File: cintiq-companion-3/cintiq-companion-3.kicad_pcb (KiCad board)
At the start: 2 copper layers, 6 parts, among them J3 13HD_buttonboard, X1 13HD_eDP, X2 13HD_penpanel

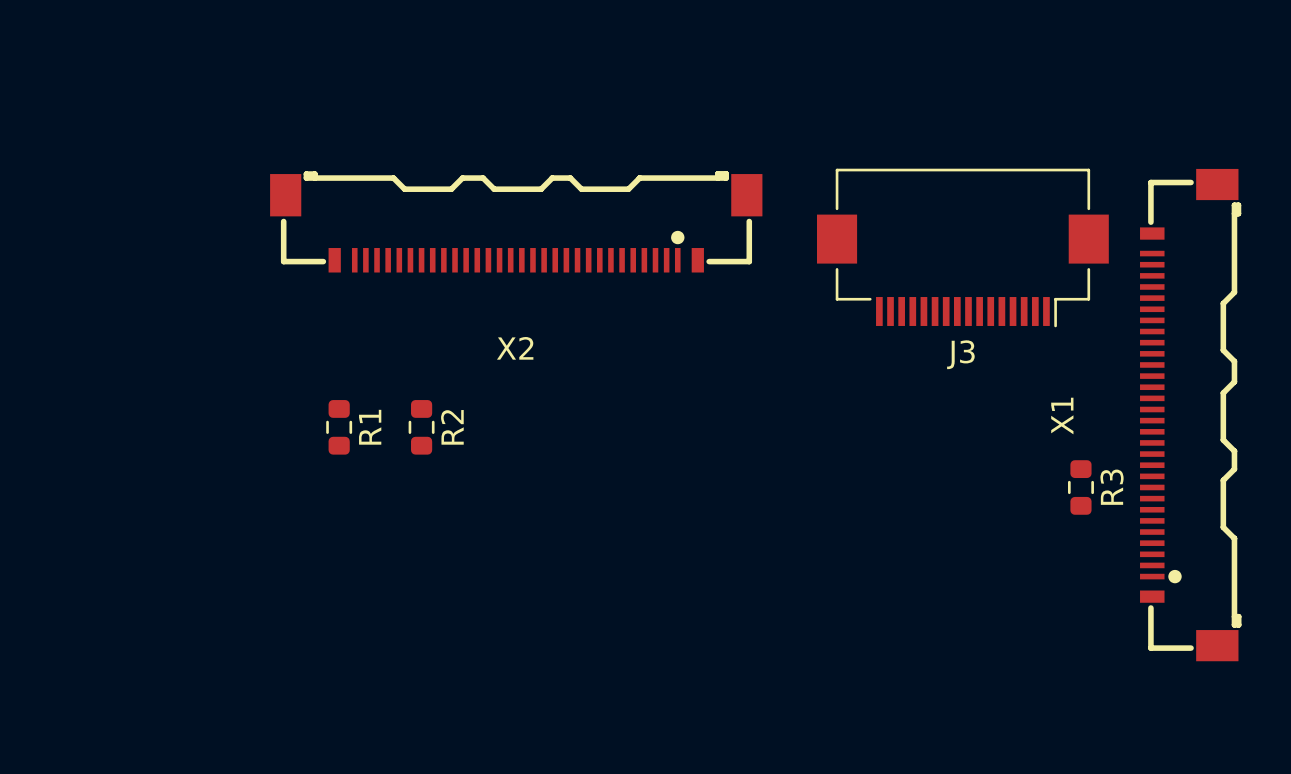
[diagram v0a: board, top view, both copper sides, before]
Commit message: Added touch panel USB footprint
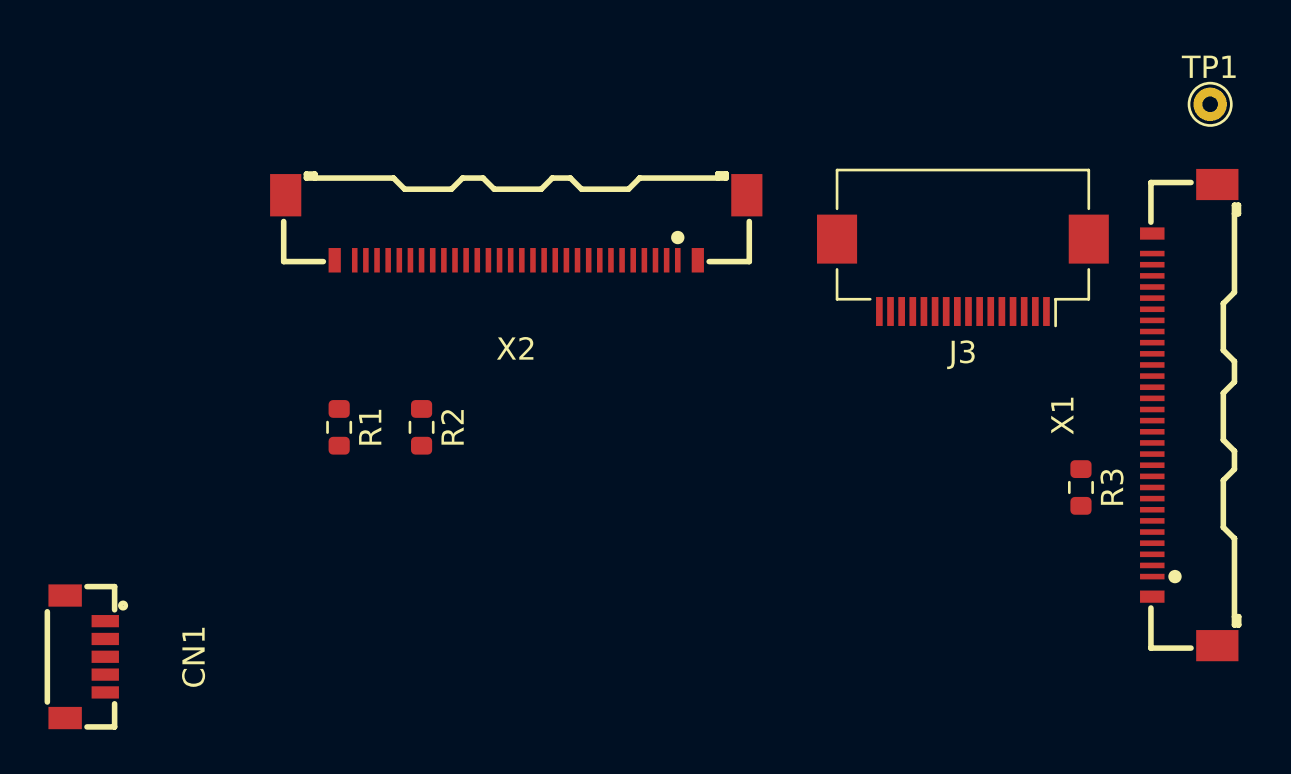
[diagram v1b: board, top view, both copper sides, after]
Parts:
- added CN1: 13HD_fingerpanel, A_my_stuff:minitek5p0.8mm, F.Cu at (144.9, 96.9)
- added TP1: Something, TestPoint:TestPoint_THTPad_D1.5mm_Drill0.7mm, F.Cu at (195.4, 72.1)

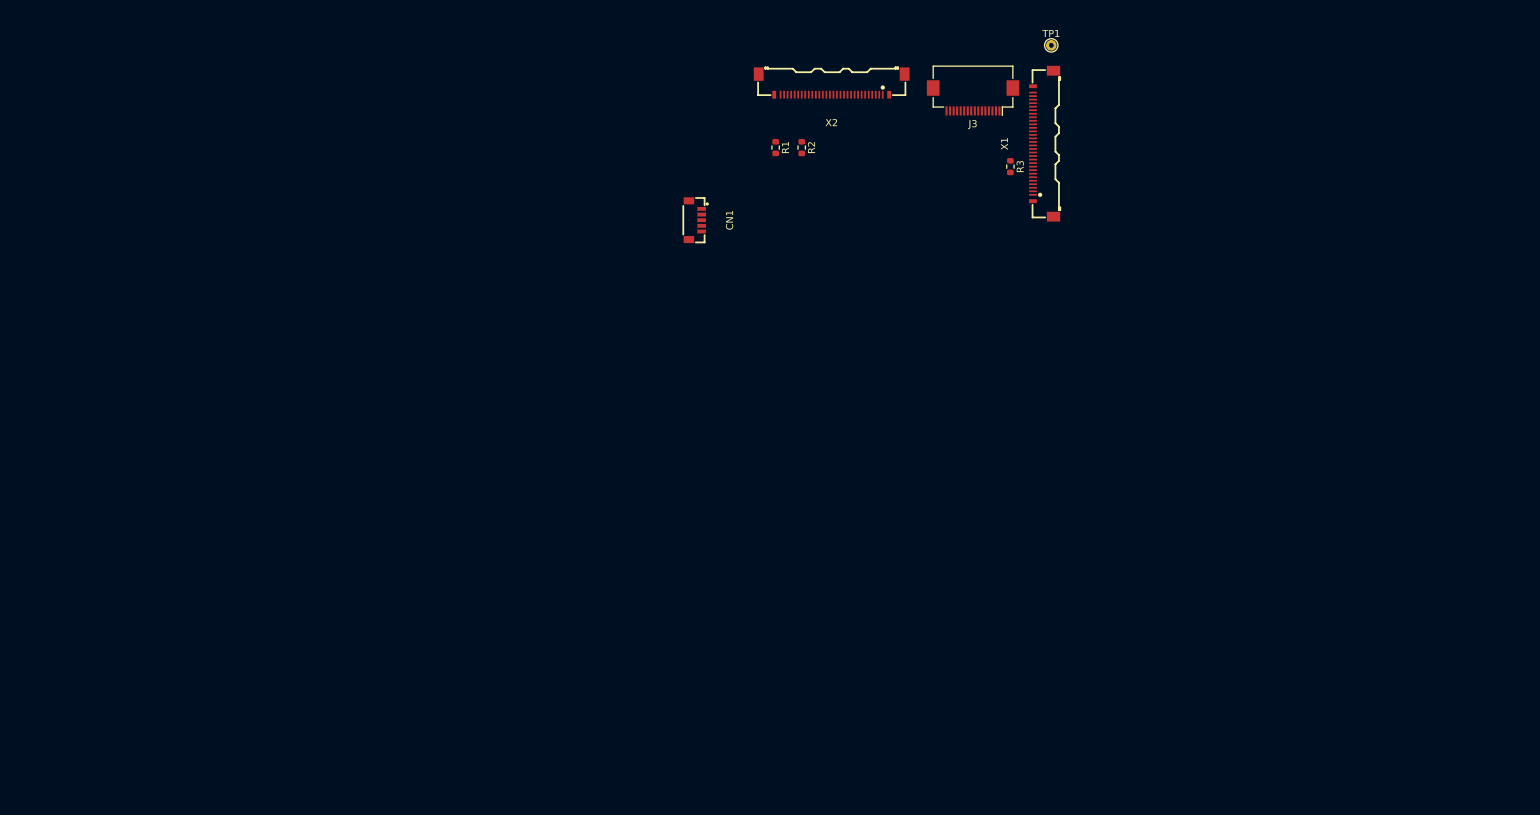
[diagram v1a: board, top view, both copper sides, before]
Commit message: Approximate connector placement done
Big board :skull:
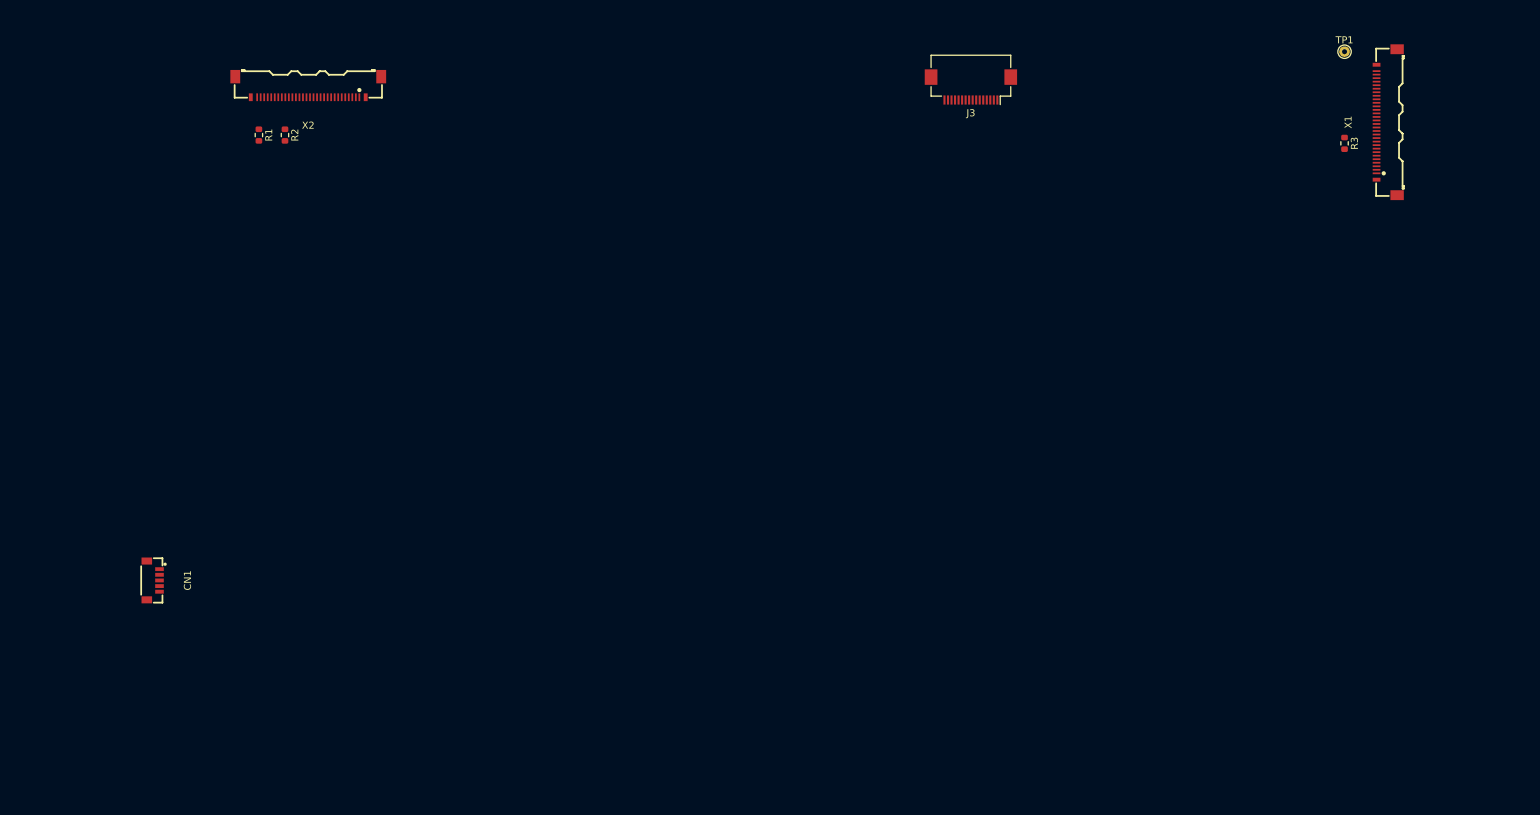
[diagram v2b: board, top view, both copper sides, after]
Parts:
- moved CN1 92.3 mm to (68.0, 148.0)
- moved X2 74.3 mm to (90.0, 78.0)
- moved R1 73.3 mm to (83.0, 84.8)
- moved R2 73.3 mm to (86.7, 84.8)
- moved X1 48.8 mm to (243.0, 83.0)
- moved R3 47.5 mm to (237.0, 86.0)
- moved TP1 41.6 mm to (237.0, 73.0)
- moved J3 1.58 mm to (184.0, 78.0)
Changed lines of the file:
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@@
 	(footprint "TestPoint:TestPoint_THTPad_D1.5mm_Drill0.7mm"
 		(layer "F.Cu")
-		(at 195.4 72.1)
+		(at 237 73)
 		(descr "THT pad as test Point, diameter 1.5mm, hole diameter 0.7mm")
 		(tags "test point THT pad")
@@
 	(footprint "Resistor_SMD:R_0603_1608Metric"
 		(layer "F.Cu")
-		(at 189.6 89.3 -90)
+		(at 237 86 -90)
 		(descr "Resistor SMD 0603 (1608 Metric), square (rectangular) end terminal, IPC_7351 nominal, (Body size source: IPC-SM-782 page 72, https://www.pcb-3d.com/wordpress/wp-content/uploads/ipc-sm-782a_amendment_1_and_2.pdf), generated with kicad-footprint-generator")
 		(tags "resistor")
@@
 	(footprint "A_my_stuff:30pipex"
 		(layer "F.Cu")
-		(at 164.25 77.64 180)
+		(at 90 78 180)
 		(property "Reference" "X2"
 			(at 0 -5.460001 180)
@@
 	(footprint "A_my_stuff:minitek5p0.8mm"
 		(layer "F.Cu")
-		(at 144.9 96.9 -90)
+		(at 68 148 -90)
 		(property "Reference" "CN1"
 			(at 0.000001 -4.9 90)
@@
 	(footprint "Resistor_SMD:R_0603_1608Metric"
 		(layer "F.Cu")
-		(at 156.3 86.6 -90)
+		(at 83 84.824999 -90)
 		(descr "Resistor SMD 0603 (1608 Metric), square (rectangular) end terminal, IPC_7351 nominal, (Body size source: IPC-SM-782 page 72, https://www.pcb-3d.com/wordpress/wp-content/uploads/ipc-sm-782a_amendment_1_and_2.pdf), generated with kicad-footprint-generator")
 		(tags "resistor")
@@
 	(footprint "A_my_stuff:30pipex"
 		(layer "F.Cu")
-		(at 194.260001 86.05 90)
+		(at 243 83 90)
 		(property "Reference" "X1"
 			(at 0.000001 -5.46 -90)
@@
 	(footprint "Connector_FFC-FPC:Hirose_FH12-16S-0.5SH_1x16-1MP_P0.50mm_Horizontal"
 		(layer "F.Cu")
-		(at 184.299999 79.549999 180)
+		(at 184 78 180)
 		(descr "Hirose FH12, FFC/FPC connector, FH12-16S-0.5SH, 16 Pins per row (https://www.hirose.com/product/en/products/FH12/FH12-24S-0.5SH(55)/), generated with kicad-footprint-generator")
 		(tags "connector Hirose FH12 horizontal")
@@
 	(footprint "Resistor_SMD:R_0603_1608Metric"
 		(layer "F.Cu")
-		(at 160 86.6 -90)
+		(at 86.7 84.824999 -90)
 		(descr "Resistor SMD 0603 (1608 Metric), square (rectangular) end terminal, IPC_7351 nominal, (Body size source: IPC-SM-782 page 72, https://www.pcb-3d.com/wordpress/wp-content/uploads/ipc-sm-782a_amendment_1_and_2.pdf), generated with kicad-footprint-generator")
 		(tags "resistor")

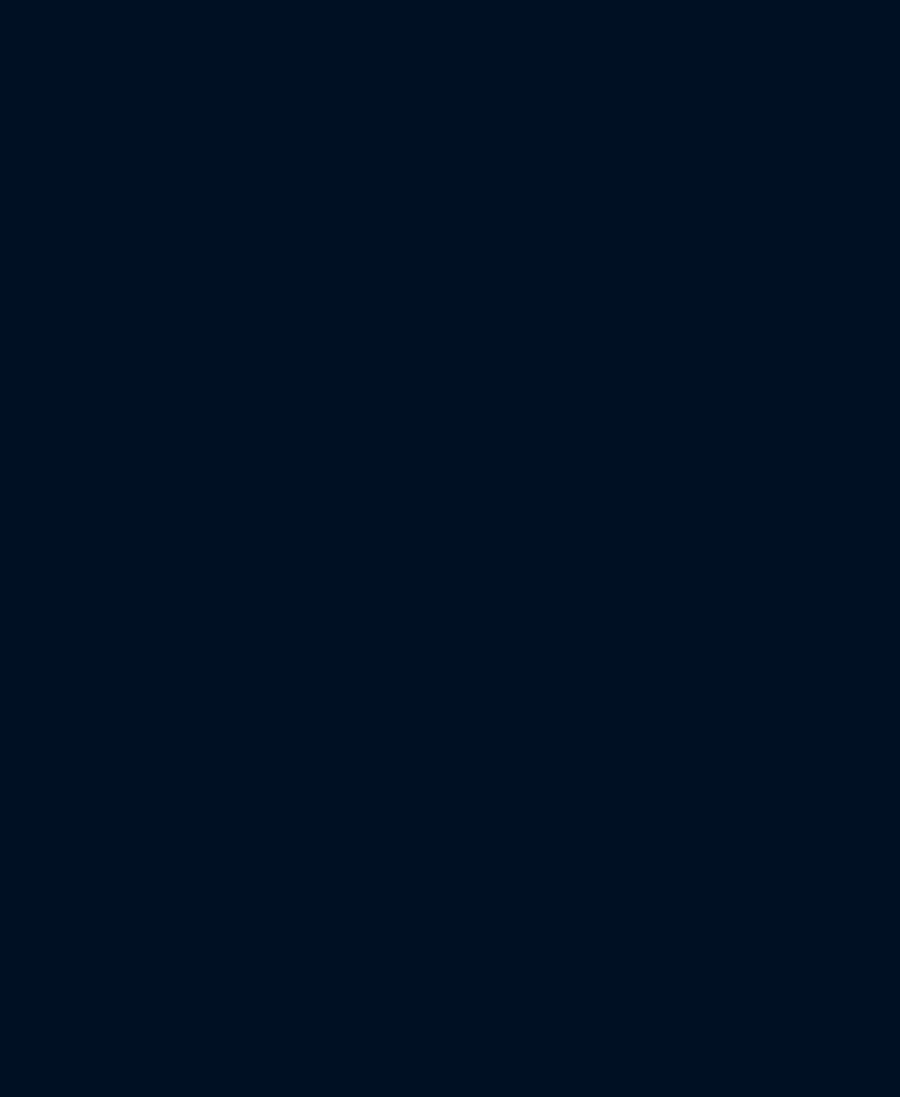
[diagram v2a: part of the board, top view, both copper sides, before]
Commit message: Added backlight controller footprint
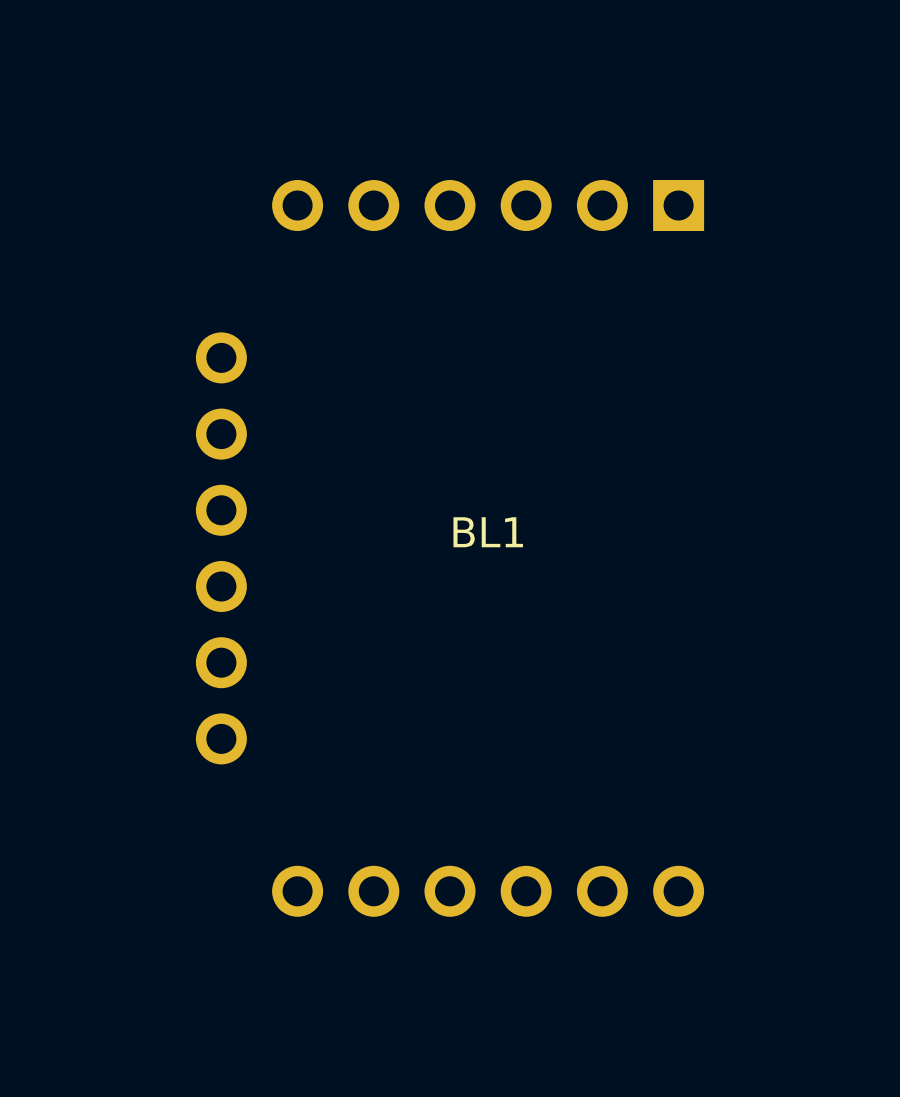
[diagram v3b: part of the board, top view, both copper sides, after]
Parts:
- added BL1: ~, A_my_stuff:koyomi-backlight, F.Cu at (168.7, 117.6)
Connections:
- net +46V_BL renamed +VBL

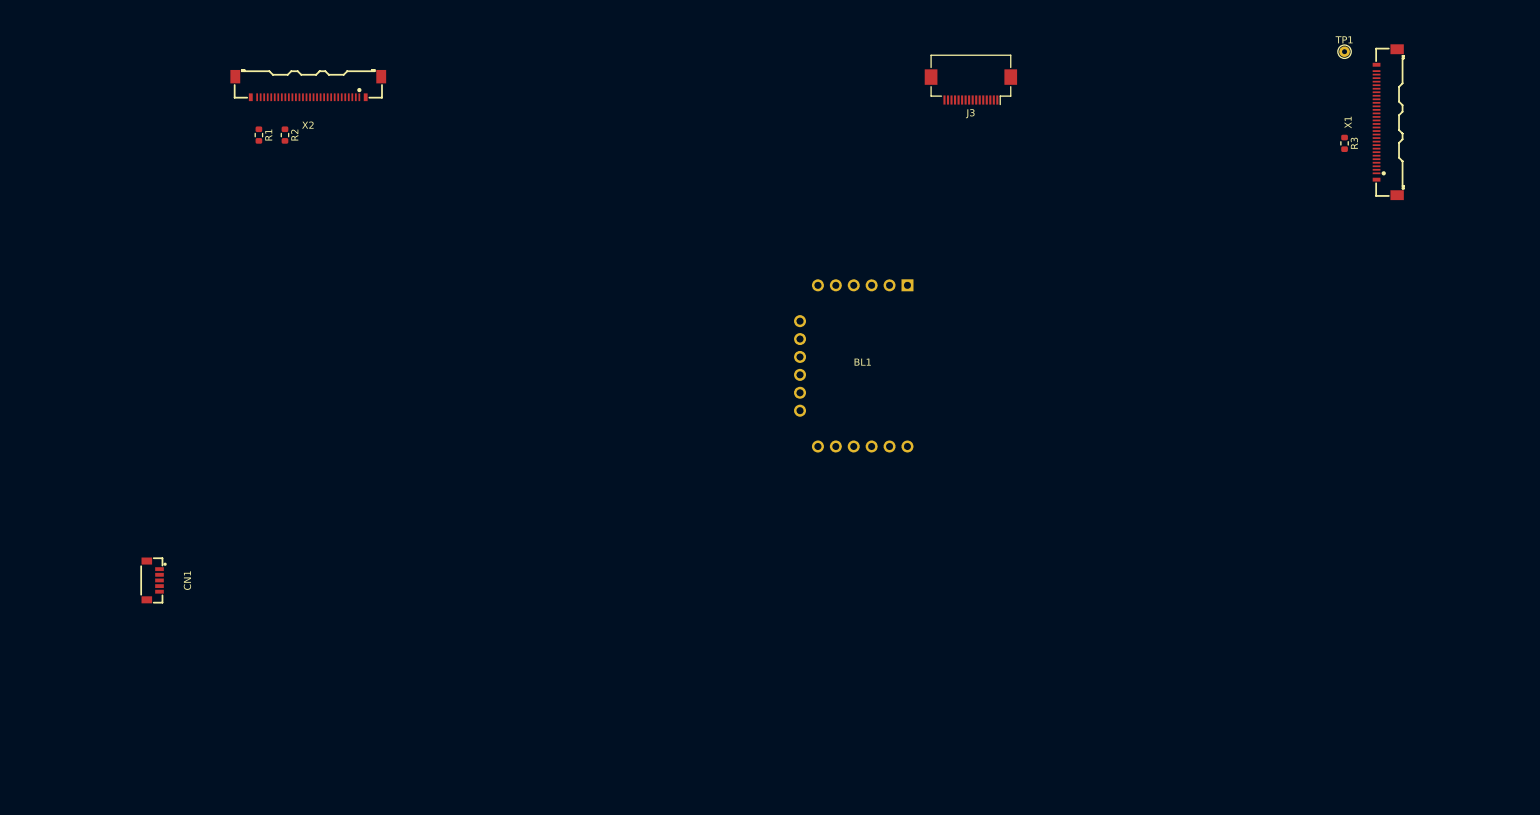
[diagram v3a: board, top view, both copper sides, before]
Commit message: Placed mount holes with image measurements but they aren't quite right
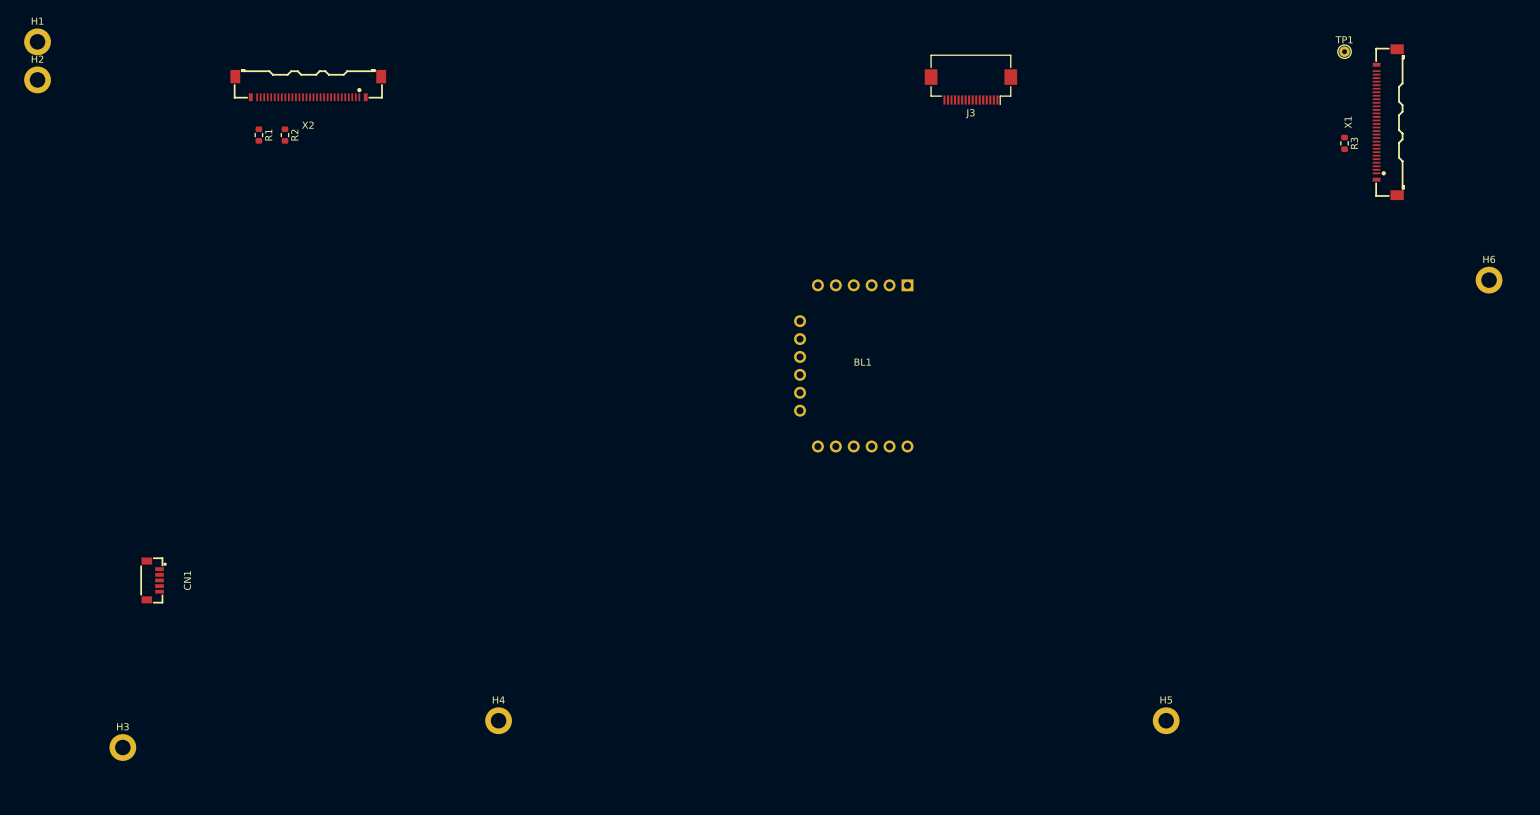
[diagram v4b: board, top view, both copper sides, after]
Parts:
- added H1: MountingHole_Pad, MountingHole:MountingHole_2.2mm_M2_DIN965_Pad, F.Cu at (51.6, 71.6)
- added H2: MountingHole_Pad, MountingHole:MountingHole_2.2mm_M2_DIN965_Pad, F.Cu at (51.6, 77.0)
- added H3: MountingHole_Pad, MountingHole:MountingHole_2.2mm_M2_DIN965_Pad, F.Cu at (63.7, 171.7)
- added H4: MountingHole_Pad, MountingHole:MountingHole_2.2mm_M2_DIN965_Pad, F.Cu at (117.0, 167.9)
- added H5: MountingHole_Pad, MountingHole:MountingHole_2.2mm_M2_DIN965_Pad, F.Cu at (211.7, 167.9)
- added H6: MountingHole_Pad, MountingHole:MountingHole_2.2mm_M2_DIN965_Pad, F.Cu at (257.5, 105.4)

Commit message: Horrible board outline
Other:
- board outline added: 214.4 x 111.3 mm
